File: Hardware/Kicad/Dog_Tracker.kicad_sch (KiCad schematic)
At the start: 20 parts

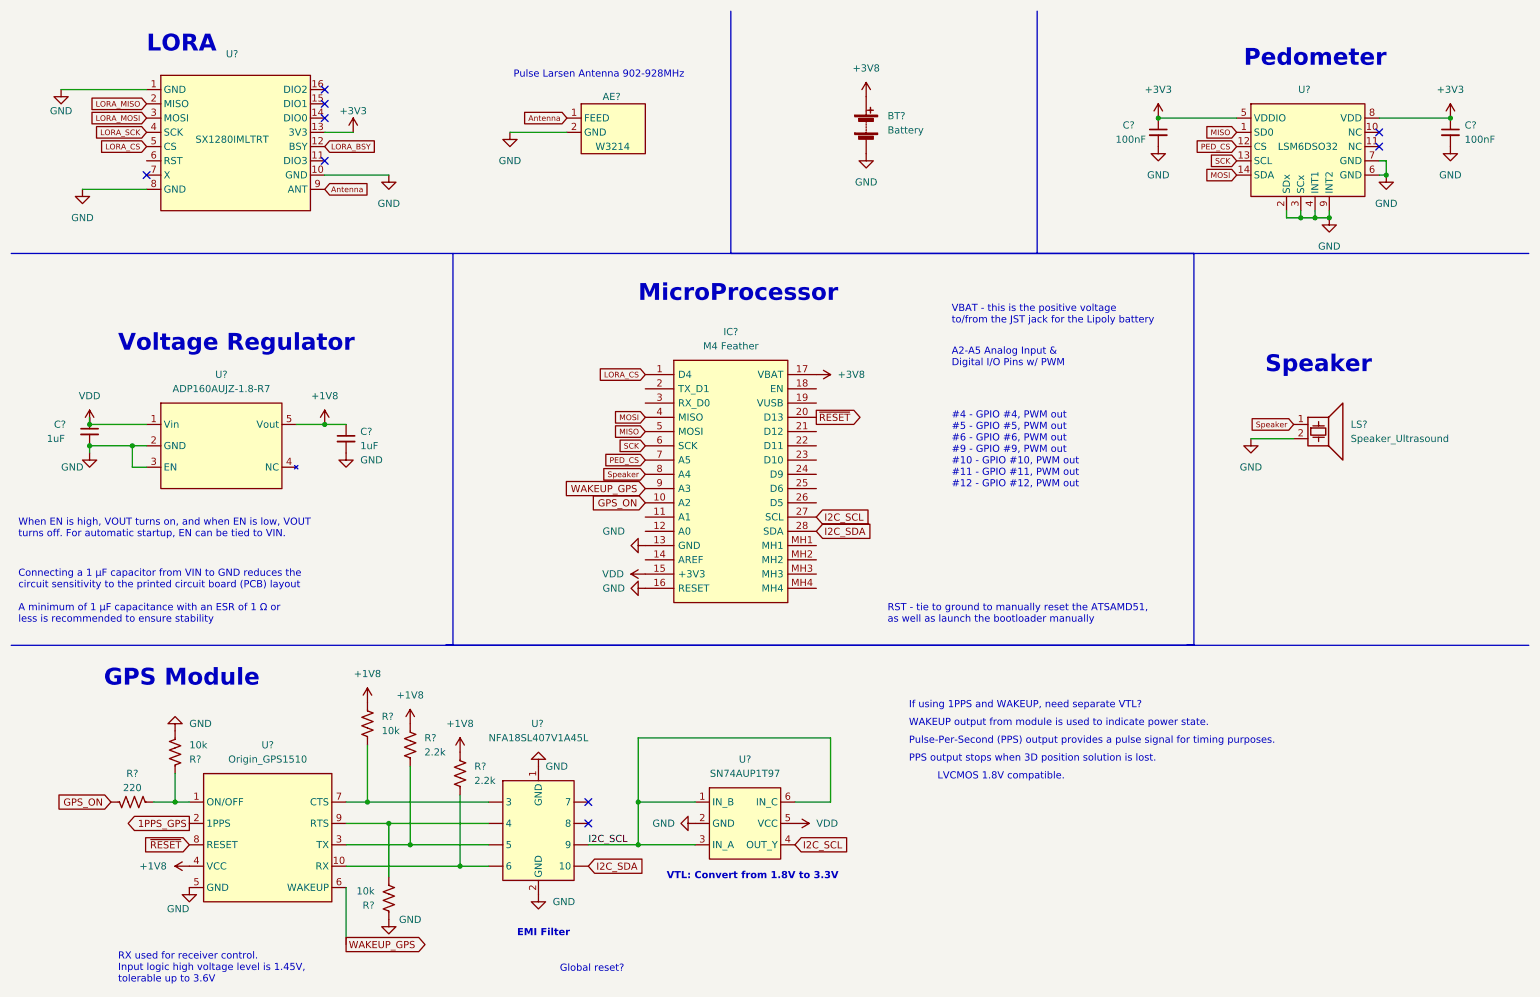
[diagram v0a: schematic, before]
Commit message: 'assigned footprints'
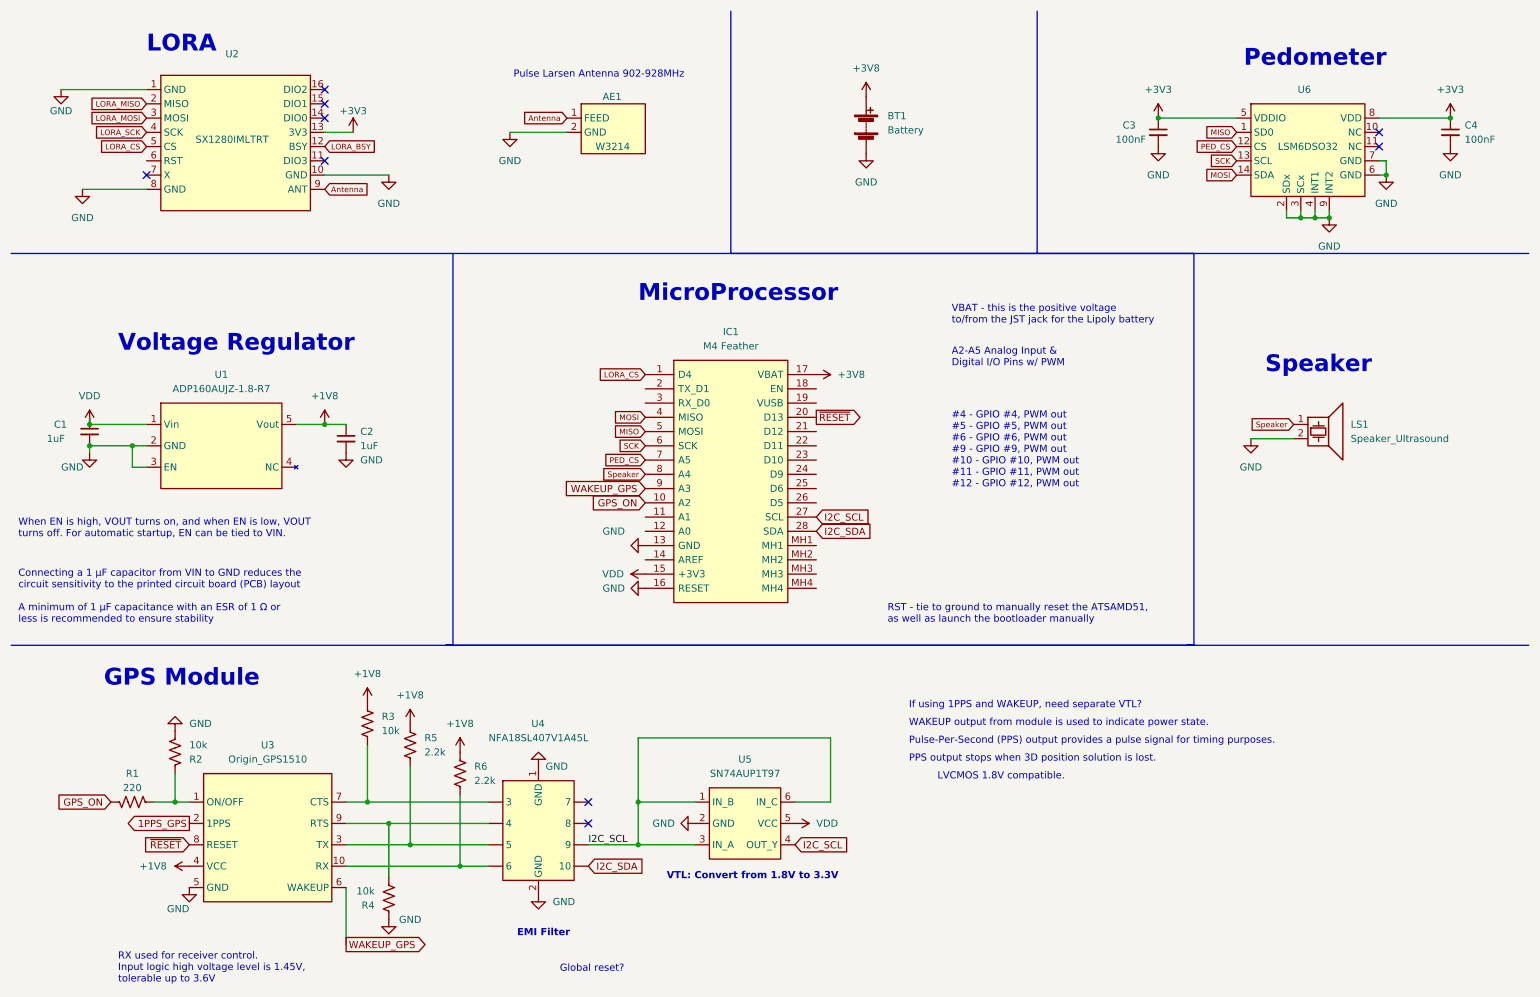
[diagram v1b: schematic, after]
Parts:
- C1, C2, C3, C4: renamed from C?; footprint (none) -> Capacitor_SMD:C_0402_1005Metric
- IC1: renamed from IC?; footprint 3857 -> Dog_Tracker:M4Feather
- R1, R2, R3, R4, R5, R6: renamed from R?; footprint (none) -> Resistor_SMD:R_0402_1005Metric
- U1: renamed from U?; footprint (none) -> Dog_Tracker:ADP160AUJZ-1.8-R7
- U2: renamed from U?; footprint (none) -> Dog_Tracker:SX1280IMLTRT
- U3: renamed from U?; footprint (none) -> Dog_Tracker:OriginGPS_LTD-ORG1510-MK04-0
- U4: renamed from U?; footprint (none) -> Dog_Tracker:NFA18SL307V1A45B
- U5: renamed from U?; footprint (none) -> Dog_Tracker:SN74AUP1T97DSFR
- gave numbers to parts that had none: 4

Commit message: update last footprint
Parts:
- U6: footprint (none) -> Dog_Tracker:LSM6DSRTR
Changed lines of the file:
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@@
     (property "Reference" "U6" (id 0) (at 243.205 26.67 0))
     (property "Value" "LSM6DSO32" (id 1) (at 243.84 36.83 0))
-    (property "Footprint" "" (id 2) (at 236.22 38.1 0)
+    (property "Footprint" "Dog_Tracker:LSM6DSRTR" (id 2) (at 236.22 38.1 0)
       (effects (font (size 1.27 1.27)) hide)
     )
@@
     )
     (path "/f5c630ac-1a2c-4b2e-a812-d252fd658f82"
-      (reference "U6") (unit 1) (value "LSM6DSO32") (footprint "")
+      (reference "U6") (unit 1) (value "LSM6DSO32") (footprint "Dog_Tracker:LSM6DSRTR")
     )
   )
